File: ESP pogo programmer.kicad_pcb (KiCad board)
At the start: 2 copper layers, 20.3 x 17.8 mm, 4 parts, among them J1 Programmer Header, U1 ESP-12F

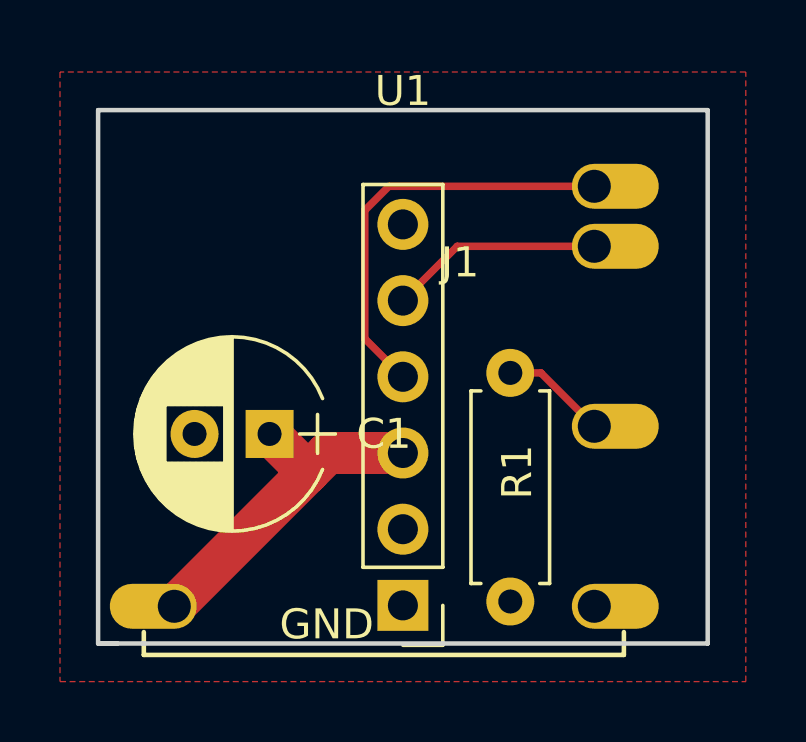
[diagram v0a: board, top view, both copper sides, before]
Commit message: adjusted track clearances to be more realistic
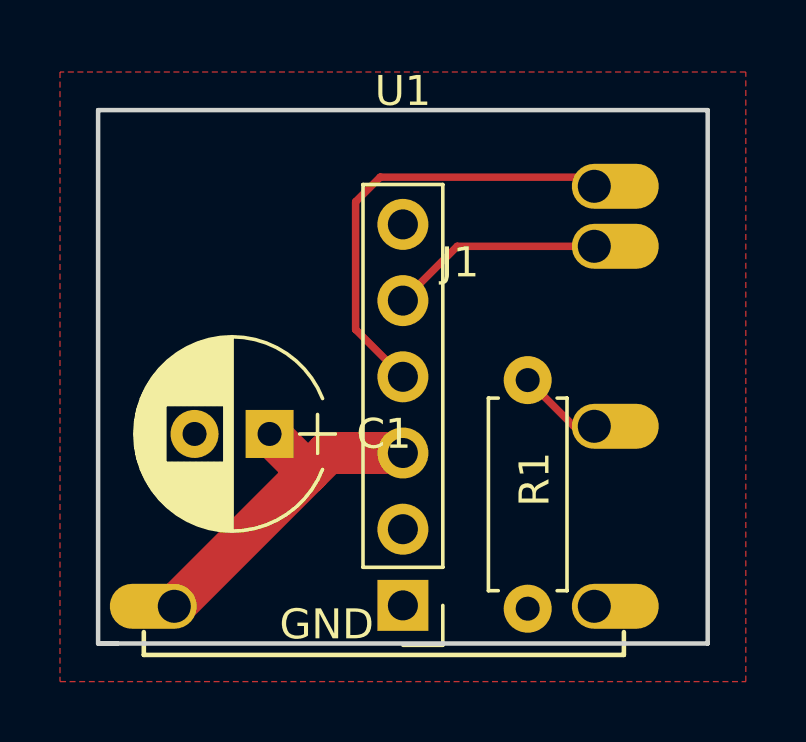
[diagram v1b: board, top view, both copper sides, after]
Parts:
- moved R1 0.63 mm to (160.4, 111.9)
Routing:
- net /PiUo: track 14.1 -> 14.9 mm
- net /GPIO0: track 3.54 -> 2.86 mm
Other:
- net class Default: clearance 0.2 -> 0.45
- net class Power: clearance 0.2 -> 0.45
- rule trace_clearance: 0.2 -> 0.45
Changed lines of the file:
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@@
     (thickness 1.6)
     (drawings 6)
-    (tracks 12)
+    (tracks 13)
     (zones 0)
     (modules 4)
@@
     (last_trace_width 0.25)
     (user_trace_width 0.25)
-    (trace_clearance 0.2)
+    (trace_clearance 0.45)
     (zone_clearance 0.2)
     (zone_45_only yes)
@@
   (net 7 /GPIO0)
   (net_class Default "This is the default net class."
-    (clearance 0.2)
+    (clearance 0.45)
     (trace_width 0.25)
     (via_dia 0.6)
@@
   )
   (net_class Power ""
-    (clearance 0.2)
+    (clearance 0.45)
     (trace_width 1.4)
     (via_dia 0.6)
@@
   )
   (module Resistors_THT:R_Axial_DIN0207_L6.3mm_D2.5mm_P7.62mm_Horizontal (layer F.Cu)
-    (at 159.79 111.63 270)
+    (at 160.37 111.87 270)
     (descr "Resistor, Axial_DIN0207 series, Axial, Horizontal, pin pitch=7.62mm, 0.25W = 1/4W, length*diameter=6.3*2.5mm^2, http://cdn-reichelt.de/documents/datenblatt/B400/1_4W%23YAG.pdf")
     (tags "Resistor Axial_DIN0207 series Axial Horizontal pin pitch 7.62mm 0.25W = 1/4W length 6.3mm diameter 2.5mm")
@@
   (segment (start 153.05 114.95) (end 153.7 114.3) (width 1.4) (layer F.Cu) (net 1))
   (segment (start 153.7 114.3) (end 156.21 114.3) (width 1.4) (layer F.Cu) (net 1))
-  (segment (start 156.21 111.76) (end 154.94 110.49) (width 0.25) (layer F.Cu) (net 4))
-  (segment (start 154.94 110.49) (end 154.94 106.210998) (width 0.25) (layer F.Cu) (net 4))
-  (segment (start 154.94 106.210998) (end 155.740998 105.41) (width 0.25) (layer F.Cu) (net 4))
-  (segment (start 155.740998 105.41) (end 162.59 105.41) (width 0.25) (layer F.Cu) (net 4) (status 20))
+  (segment (start 156.21 111.76) (end 154.634999 110.184999) (width 0.25) (layer F.Cu) (net 4))
+  (segment (start 154.634999 110.184999) (end 154.634999 105.923999) (width 0.25) (layer F.Cu) (net 4))
+  (segment (start 155.453999 105.104999) (end 162.284999 105.104999) (width 0.25) (layer F.Cu) (net 4))
+  (segment (start 154.634999 105.923999) (end 155.453999 105.104999) (width 0.25) (layer F.Cu) (net 4))
+  (segment (start 162.284999 105.104999) (end 162.59 105.41) (width 0.25) (layer F.Cu) (net 4))
   (segment (start 156.21 109.22) (end 158.02 107.41) (width 0.25) (layer F.Cu) (net 5))
   (segment (start 158.02 107.41) (end 162.59 107.41) (width 0.25) (layer F.Cu) (net 5) (status 20))
-  (segment (start 159.79 111.63) (end 160.81 111.63) (width 0.25) (layer F.Cu) (net 7))
-  (segment (start 160.81 111.63) (end 162.59 113.41) (width 0.25) (layer F.Cu) (net 7) (status 20))
+  (segment (start 160.37 111.87) (end 161.91 113.41) (width 0.25) (layer F.Cu) (net 7))
+  (segment (start 161.91 113.41) (end 162.59 113.41) (width 0.25) (layer F.Cu) (net 7))
   (zone (net 2) (net_name GND) (layer F.Cu) (hatch edge 0.508)
     (connect_pads yes (clearance 0.2))
-    (min_thickness 1.1)
+    (min_thickness 0.2)
     (fill yes (arc_segments 16) (thermal_gap 0.508) (thermal_bridge_width 1.101))
     (polygon

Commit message: swapped false pins in PCBnew
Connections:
- J1 pad 4: /PiUo -> /PoUi
- J1 pad 5: /PoUi -> /PiUo
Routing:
- net /PiUo: track 14.9 -> 8.39 mm
- net /PoUi: track 7.13 -> 8.18 mm
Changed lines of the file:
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@@
     (links 8)
     (no_connects 0)
-    (area 144.78 96.434999 167.640001 121.920001)
+    (area 145.974999 102.794999 166.445001 120.725001)
     (thickness 1.6)
     (drawings 6)
-    (tracks 13)
+    (tracks 11)
     (zones 0)
     (modules 4)
@@
       (net 1 VCC))
     (pad 4 thru_hole oval (at 0 7.62 180) (size 1.7 1.7) (drill 1) (layers *.Cu *.Mask)
+      (net 5 /PoUi))
+    (pad 5 thru_hole oval (at 0 10.16 180) (size 1.7 1.7) (drill 1) (layers *.Cu *.Mask)
       (net 4 /PiUo))
-    (pad 5 thru_hole oval (at 0 10.16 180) (size 1.7 1.7) (drill 1) (layers *.Cu *.Mask)
-      (net 5 /PoUi))
     (pad 6 thru_hole oval (at 0 12.7 180) (size 1.7 1.7) (drill 1) (layers *.Cu *.Mask)
       (net 6 /DTR))
@@
   (segment (start 153.05 114.95) (end 153.7 114.3) (width 1.4) (layer F.Cu) (net 1))
   (segment (start 153.7 114.3) (end 156.21 114.3) (width 1.4) (layer F.Cu) (net 1))
-  (segment (start 156.21 111.76) (end 154.634999 110.184999) (width 0.25) (layer F.Cu) (net 4))
-  (segment (start 154.634999 110.184999) (end 154.634999 105.923999) (width 0.25) (layer F.Cu) (net 4))
-  (segment (start 155.453999 105.104999) (end 162.284999 105.104999) (width 0.25) (layer F.Cu) (net 4))
-  (segment (start 154.634999 105.923999) (end 155.453999 105.104999) (width 0.25) (layer F.Cu) (net 4))
+  (segment (start 162.59 105.41) (end 160.02 105.41) (width 0.25) (layer F.Cu) (net 4))
+  (segment (start 160.02 105.41) (end 156.21 109.22) (width 0.25) (layer F.Cu) (net 4))
   (segment (start 162.284999 105.104999) (end 162.59 105.41) (width 0.25) (layer F.Cu) (net 4))
-  (segment (start 156.21 109.22) (end 158.02 107.41) (width 0.25) (layer F.Cu) (net 5))
-  (segment (start 158.02 107.41) (end 162.59 107.41) (width 0.25) (layer F.Cu) (net 5) (status 20))
+  (segment (start 162.59 107.41) (end 160.56 107.41) (width 0.25) (layer F.Cu) (net 5))
+  (segment (start 160.56 107.41) (end 156.21 111.76) (width 0.25) (layer F.Cu) (net 5))
   (segment (start 160.37 111.87) (end 161.91 113.41) (width 0.25) (layer F.Cu) (net 7))
   (segment (start 161.91 113.41) (end 162.59 113.41) (width 0.25) (layer F.Cu) (net 7))

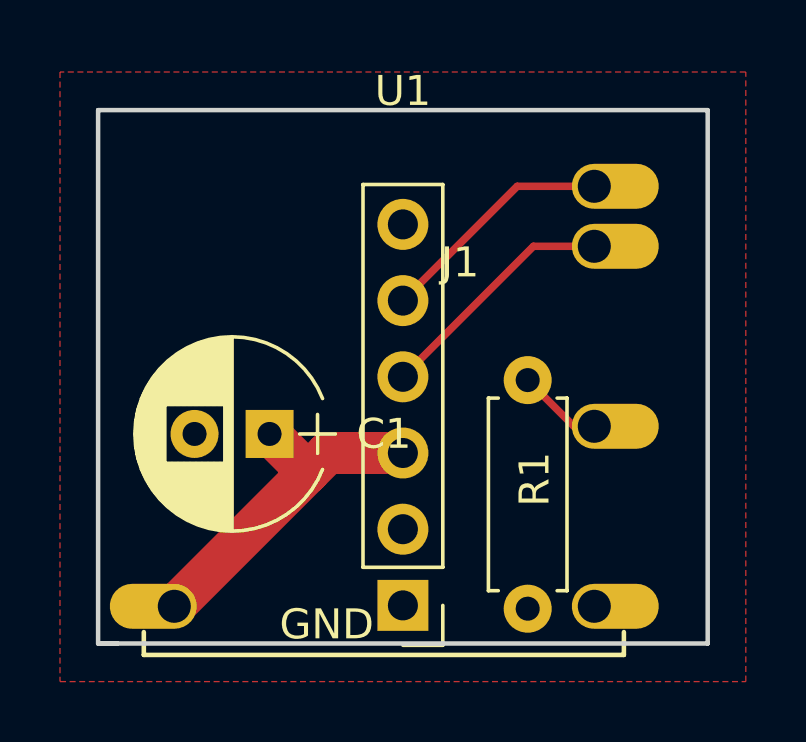
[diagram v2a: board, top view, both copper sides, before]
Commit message: flipped ESP-12 so its is correct way round
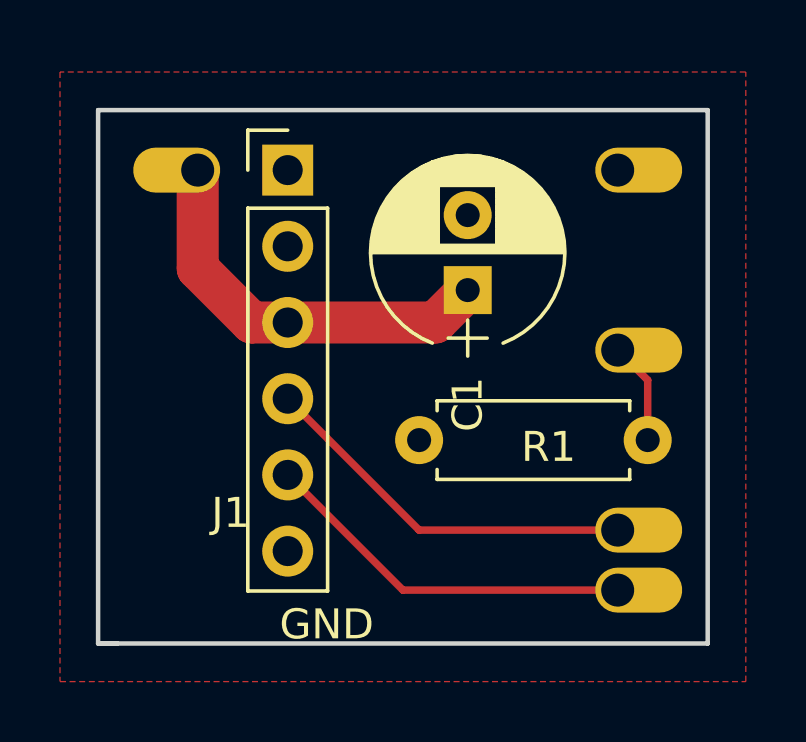
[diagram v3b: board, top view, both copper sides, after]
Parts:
- U1: moved to B.Cu
- moved J1 15.0 mm to (152.4, 104.9), turned to 0 degrees
- moved U1 13.5 mm to (149.4, 118.9)
- moved C1 8.16 mm to (158.4, 108.9), turned to 90 degrees
- moved R1 4.47 mm to (164.4, 113.9), turned to 180 degrees
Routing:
- net /PoUi: track 8.18 -> 12.8 mm
- net /PiUo: track 8.39 -> 12.6 mm
- net VCC: track 11.6 -> 13.5 mm
- net /GPIO0: track 2.86 -> 3.41 mm

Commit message: small changes
changed edge cut width and position slightly. moved origin to new top right corner.
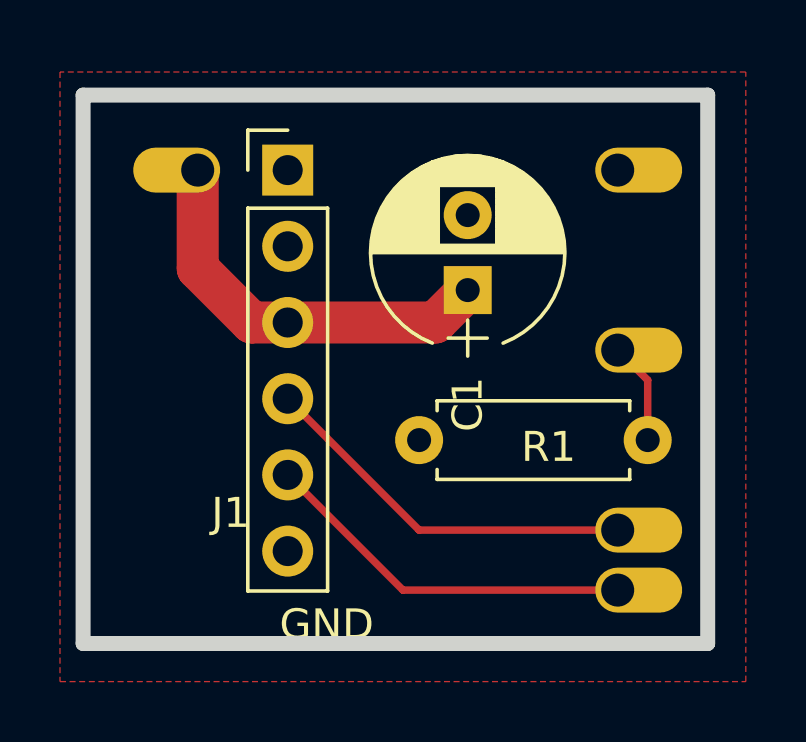
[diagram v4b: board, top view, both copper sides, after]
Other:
- board size 20.3 x 17.8 mm -> 20.8 x 18.3 mm
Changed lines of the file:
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@@
     (trace_min 0.2)
     (segment_width 0.2)
-    (edge_width 0.15)
+    (edge_width 0.5)
     (via_size 0.6)
     (via_drill 0.4)
@@
     (pad_drill 0.762)
     (pad_to_mask_clearance 0.2)
-    (aux_axis_origin 169.37 99.87)
-    (grid_origin 166.37 102.87)
+    (aux_axis_origin 166.37 102.37)
+    (grid_origin 166.37 102.37)
     (visible_elements 7FFFFFFF)
     (pcbplotparams
@@
   )
   (gr_line (start 146.05 120.65) (end 146.685 120.65) (angle 90) (layer Edge.Cuts) (width 0.15))
-  (gr_line (start 146.05 102.87) (end 146.05 120.65) (angle 90) (layer Edge.Cuts) (width 0.15))
-  (gr_line (start 166.37 102.87) (end 146.05 102.87) (angle 90) (layer Edge.Cuts) (width 0.15))
-  (gr_line (start 166.37 120.65) (end 166.37 102.87) (angle 90) (layer Edge.Cuts) (width 0.15))
-  (gr_line (start 146.05 120.65) (end 166.37 120.65) (angle 90) (layer Edge.Cuts) (width 0.15))
+  (gr_line (start 145.55 102.37) (end 145.55 120.65) (angle 90) (layer Edge.Cuts) (width 0.5))
+  (gr_line (start 166.37 102.37) (end 145.55 102.37) (angle 90) (layer Edge.Cuts) (width 0.5))
+  (gr_line (start 166.37 120.65) (end 166.37 102.37) (angle 90) (layer Edge.Cuts) (width 0.5))
+  (gr_line (start 145.55 120.65) (end 166.37 120.65) (angle 90) (layer Edge.Cuts) (width 0.5))
   (gr_text GND (at 153.67 120.015) (layer F.SilkS)
     (effects (font (size 1 1) (thickness 0.15)))
@@
   (zone (net 2) (net_name GND) (layer F.Cu) (hatch edge 0.508)
     (connect_pads yes (clearance 0.2))
-    (min_thickness 0.2)
+    (min_thickness 0.25)
     (fill yes (arc_segments 16) (thermal_gap 0.508) (thermal_bridge_width 1.101))
     (polygon

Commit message: moved capacitor down slightly
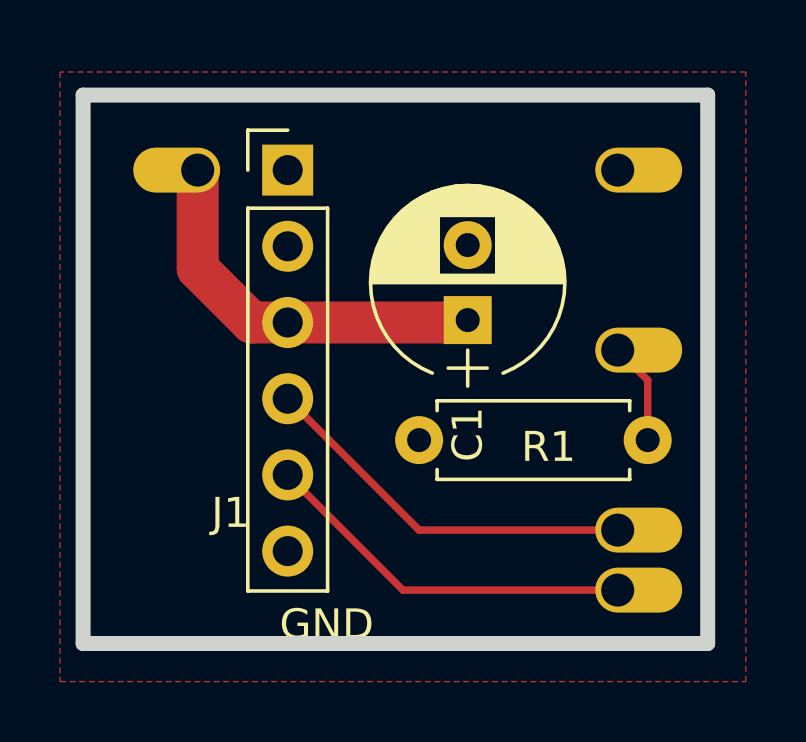
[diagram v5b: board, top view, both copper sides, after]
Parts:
- moved C1 1.00 mm to (158.4, 109.9)
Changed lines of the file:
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@@
   )
   (module Capacitors_THT:CP_Radial_D6.3mm_P2.50mm (layer F.Cu)
-    (at 158.37 108.87 90)
+    (at 158.37 109.87 90)
     (descr "CP, Radial series, Radial, pin pitch=2.50mm, , diameter=6.3mm, Electrolytic Capacitor")
     (tags "CP Radial series Radial pin pitch 2.50mm  diameter 6.3mm Electrolytic Capacitor")
@@
     (effects (font (size 1 1) (thickness 0.15)))
   )
-  (segment (start 152.37 109.95) (end 157.29 109.95) (width 1.4) (layer F.Cu) (net 1))
-  (segment (start 157.29 109.95) (end 158.37 108.87) (width 1.4) (layer F.Cu) (net 1))
+  (segment (start 152.37 109.95) (end 158.29 109.95) (width 1.4) (layer F.Cu) (net 1) (status C00000))
+  (segment (start 158.29 109.95) (end 158.37 109.87) (width 1.4) (layer F.Cu) (net 1) (status C00000))
   (segment (start 149.37 104.87) (end 149.37 108.152081) (width 1.4) (layer F.Cu) (net 1))
   (segment (start 149.37 108.152081) (end 151.167919 109.95) (width 1.4) (layer F.Cu) (net 1))
